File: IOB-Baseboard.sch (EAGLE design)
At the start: 72 parts, among them J1 I2C, J2 I2C, Q0 P-FET, Q1 P-FET, Q10 P-FET, Q11 P-FET, Q12 P-FET, Q13 P-FET, Q14 P-FET, Q15 P-FET, Q2 P-FET, Q3 P-FET, Q4 P-FET, Q5 P-FET, Q6 P-FET, Q7 P-FET, Q8 P-FET, Q9 P-FET

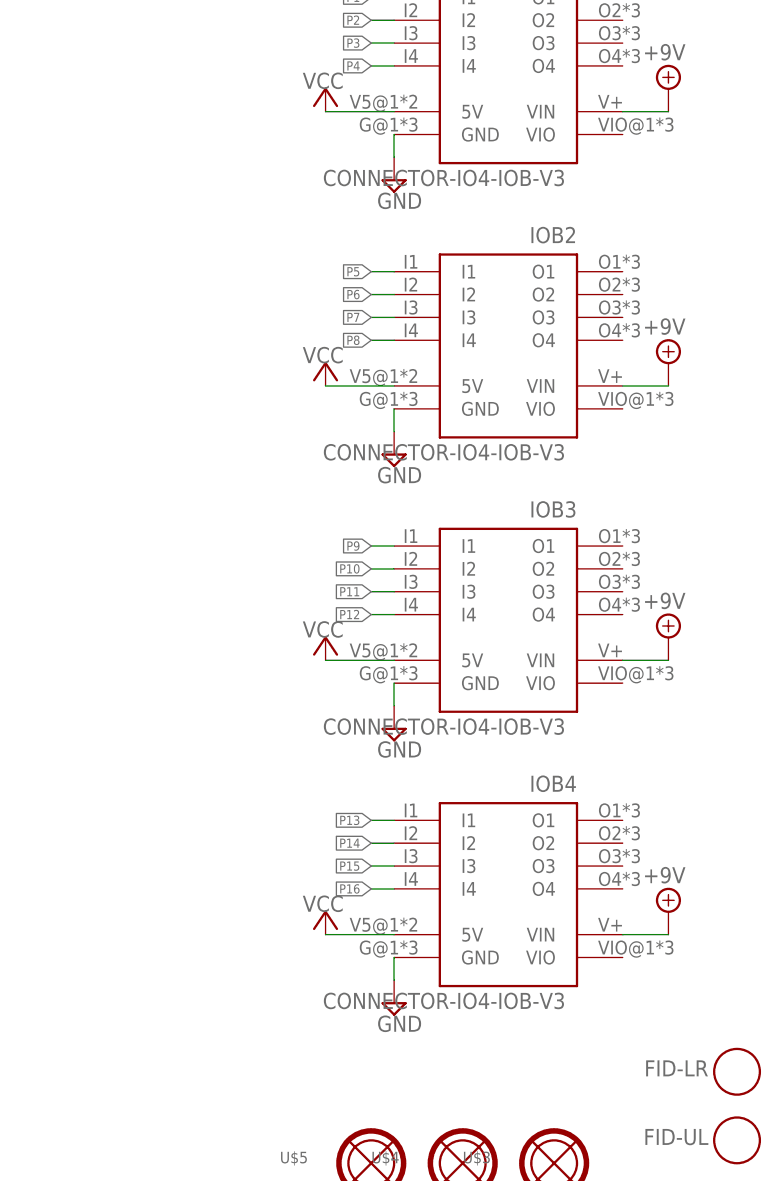
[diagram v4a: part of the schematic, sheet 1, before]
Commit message: normalized values
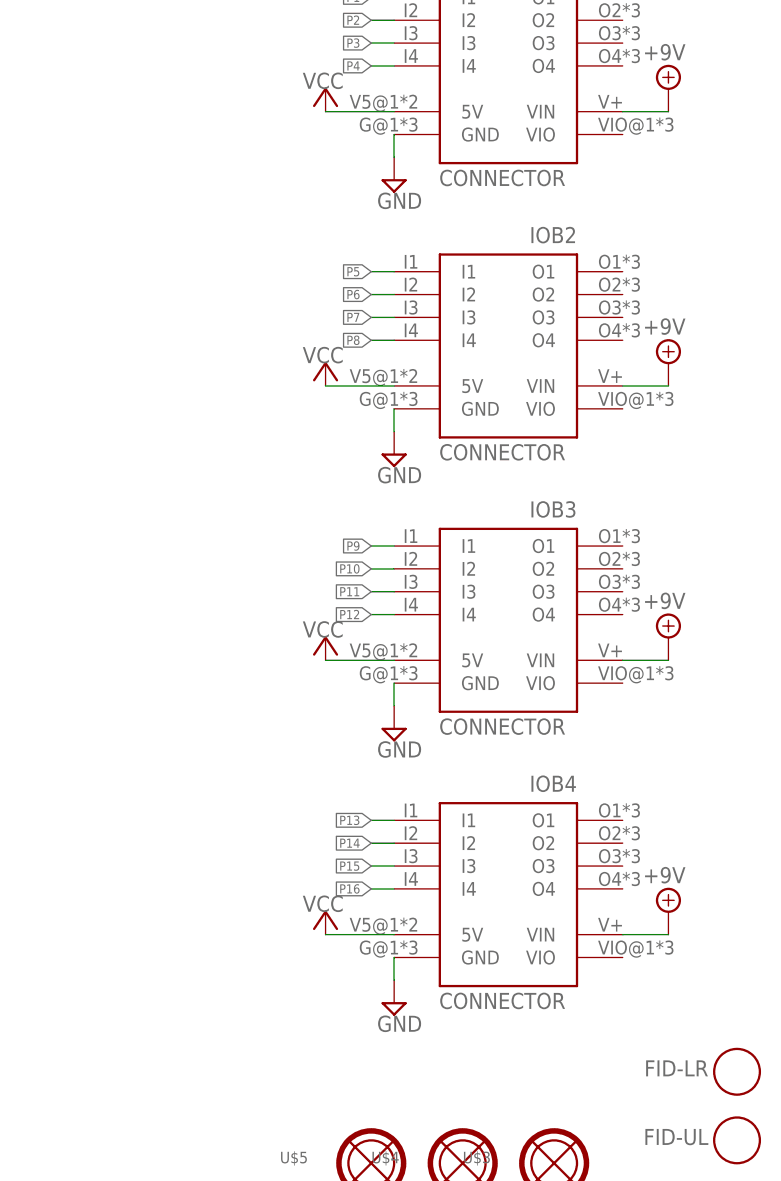
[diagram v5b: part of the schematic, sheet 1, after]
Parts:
- BOARD1: value BOARD80X100-IOB -> BOARD
- C1, C2: device SPCoast:CAP0805 -> SPCoast:CAP0603
- IOB1, IOB2, IOB3, IOB4: value CONNECTOR-IO4-IOB-V3 -> CONNECTOR
- R10, R11, R12, R13, R14, R15, R16, R18, R2, R21, R22, R4, R5, R6, R7, R8, R9: device SPCoast:R0805-RES -> SPCoast:R0603-RES
- U$1: value OSHW-LOGOL -> OSHW
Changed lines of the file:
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@@
 <parts>
 <part name="FRAME1" library="MCP" deviceset="FRAME-LETTER" device=""/>
-<part name="C1" library="SPCoast" deviceset="CAP*" device="0805" value="0.1uF"/>
-<part name="C2" library="SPCoast" deviceset="CAP*" device="0805" value="10uF"/>
+<part name="C1" library="SPCoast" deviceset="CAP*" device="0603" value="0.1uF"/>
+<part name="C2" library="SPCoast" deviceset="CAP*" device="0603" value="10uF"/>
 <part name="P+2" library="supply1" deviceset="VCC" device=""/>
-<part name="U$1" library="SparkFun" deviceset="OSHW-LOGO" device="L" value="OSHW-LOGOL"/>
+<part name="U$1" library="SparkFun" deviceset="OSHW-LOGO" device="L" value="OSHW"/>
 <part name="V1" library="supply2" deviceset="GND" device=""/>
 <part name="VR1" library="SPCoast" deviceset="VREG-?-*" device="DPAK" technology="5" value="CJ7805"/>
-<part name="R18" library="SPCoast" deviceset="R*" device="0805-RES" value="2K0"/>
+<part name="R18" library="SPCoast" deviceset="R*" device="0603-RES" value="2K0"/>
 <part name="LED18" library="SPCoast" deviceset="LED*" device="0603-LED" value="G"/>
 <part name="SUPPLY2" library="supply2" deviceset="+9V" device=""/>
@@
 <part name="J2" library="SPCoast" deviceset="CONNECTOR-I2C" device="LEFT" value="I2C"/>
 <part name="V12" library="supply2" deviceset="GND" device=""/>
-<part name="BOARD1" library="SPCoast" deviceset="BOARD" device="80X100-IOB" value="BOARD80X100-IOB"/>
+<part name="BOARD1" library="SPCoast" deviceset="BOARD" device="80X100-IOB" value="BOARD"/>
 <part name="P+3" library="supply1" deviceset="VCC" device=""/>
 <part name="V9" library="supply2" deviceset="GND" device=""/>
@@
 <part name="VIN1" library="SPCoast" deviceset="CONNECTOR-POWER" device="-L"/>
 <part name="VIN2" library="SPCoast" deviceset="CONNECTOR-POWER" device="-L" value="CONNECTOR-POWER-L"/>
-<part name="IOB1" library="SPCoast" deviceset="CONNECTOR-IO4-IOB-V3" device=""/>
+<part name="IOB1" library="SPCoast" deviceset="CONNECTOR-IO4-IOB-V3" device="" value="CONNECTOR"/>
 <part name="P+4" library="supply1" deviceset="VCC" device=""/>
 <part name="V2" library="supply2" deviceset="GND" device=""/>
 <part name="SUPPLY1" library="supply2" deviceset="+9V" device=""/>
-<part name="IOB2" library="SPCoast" deviceset="CONNECTOR-IO4-IOB-V3" device=""/>
+<part name="IOB2" library="SPCoast" deviceset="CONNECTOR-IO4-IOB-V3" device="" value="CONNECTOR"/>
 <part name="P+5" library="supply1" deviceset="VCC" device=""/>
 <part name="V3" library="supply2" deviceset="GND" device=""/>
 <part name="SUPPLY4" library="supply2" deviceset="+9V" device=""/>
-<part name="IOB3" library="SPCoast" deviceset="CONNECTOR-IO4-IOB-V3" device=""/>
+<part name="IOB3" library="SPCoast" deviceset="CONNECTOR-IO4-IOB-V3" device="" value="CONNECTOR"/>
 <part name="P+7" library="supply1" deviceset="VCC" device=""/>
 <part name="V4" library="supply2" deviceset="GND" device=""/>
 <part name="SUPPLY5" library="supply2" deviceset="+9V" device=""/>
-<part name="IOB4" library="SPCoast" deviceset="CONNECTOR-IO4-IOB-V3" device=""/>
+<part name="IOB4" library="SPCoast" deviceset="CONNECTOR-IO4-IOB-V3" device="" value="CONNECTOR"/>
 <part name="U$2" library="SPCoast" deviceset="CONNECTOR-I2C-EXPANDER" device=""/>
 <part name="V6" library="supply2" deviceset="GND" device=""/>
@@
 <part name="FRAME3" library="SPCoast" deviceset="DOC-FRAME-LETTER" device=""/>
 <part name="LED2" library="SPCoast" deviceset="LED*" device="0603-LED" value="Y"/>
-<part name="R4" library="SPCoast" deviceset="R*" device="0805-RES" value="2K0"/>
+<part name="R4" library="SPCoast" deviceset="R*" device="0603-RES" value="2K0"/>
 <part name="LED3" library="SPCoast" deviceset="LED*" device="0603-LED" value="Y"/>
-<part name="R5" library="SPCoast" deviceset="R*" device="0805-RES" value="2K0"/>
+<part name="R5" library="SPCoast" deviceset="R*" device="0603-RES" value="2K0"/>
 <part name="LED4" library="SPCoast" deviceset="LED*" device="0603-LED" value="Y"/>
-<part name="R6" library="SPCoast" deviceset="R*" device="0805-RES" value="2K0"/>
+<part name="R6" library="SPCoast" deviceset="R*" device="0603-RES" value="2K0"/>
 <part name="LED5" library="SPCoast" deviceset="LED*" device="0603-LED" value="Y"/>
-<part name="R7" library="SPCoast" deviceset="R*" device="0805-RES" value="2K0"/>
+<part name="R7" library="SPCoast" deviceset="R*" device="0603-RES" value="2K0"/>
 <part name="Q0" library="SPCoast" deviceset="MOSFET-P" device="-044021001" value="P-FET"/>
 <part name="Q1" library="SPCoast" deviceset="MOSFET-P" device="-044021001" value="P-FET"/>
@@
 <part name="P+21" library="supply1" deviceset="VCC" device=""/>
 <part name="LED6" library="SPCoast" deviceset="LED*" device="0603-LED" value="Y"/>
-<part name="R8" library="SPCoast" deviceset="R*" device="0805-RES" value="2K0"/>
+<part name="R8" library="SPCoast" deviceset="R*" device="0603-RES" value="2K0"/>
 <part name="LED7" library="SPCoast" deviceset="LED*" device="0603-LED" value="Y"/>
-<part name="R9" library="SPCoast" deviceset="R*" device="0805-RES" value="2K0"/>
+<part name="R9" library="SPCoast" deviceset="R*" device="0603-RES" value="2K0"/>
 <part name="LED8" library="SPCoast" deviceset="LED*" device="0603-LED" value="Y"/>
-<part name="R10" library="SPCoast" deviceset="R*" device="0805-RES" value="2K0"/>
+<part name="R10" library="SPCoast" deviceset="R*" device="0603-RES" value="2K0"/>
 <part name="LED9" library="SPCoast" deviceset="LED*" device="0603-LED" value="Y"/>
-<part name="R11" library="SPCoast" deviceset="R*" device="0805-RES" value="2K0"/>
+<part name="R11" library="SPCoast" deviceset="R*" device="0603-RES" value="2K0"/>
 <part name="Q4" library="SPCoast" deviceset="MOSFET-P" device="-044021001" value="P-FET"/>
 <part name="Q5" library="SPCoast" deviceset="MOSFET-P" device="-044021001" value="P-FET"/>
@@
 <part name="P+25" library="supply1" deviceset="VCC" device=""/>
 <part name="LED10" library="SPCoast" deviceset="LED*" device="0603-LED" value="Y"/>
-<part name="R12" library="SPCoast" deviceset="R*" device="0805-RES" value="2K0"/>
+<part name="R12" library="SPCoast" deviceset="R*" device="0603-RES" value="2K0"/>
 <part name="LED11" library="SPCoast" deviceset="LED*" device="0603-LED" value="Y"/>
-<part name="R13" library="SPCoast" deviceset="R*" device="0805-RES" value="2K0"/>
+<part name="R13" library="SPCoast" deviceset="R*" device="0603-RES" value="2K0"/>
 <part name="LED12" library="SPCoast" deviceset="LED*" device="0603-LED" value="Y"/>
-<part name="R14" library="SPCoast" deviceset="R*" device="0805-RES" value="2K0"/>
+<part name="R14" library="SPCoast" deviceset="R*" device="0603-RES" value="2K0"/>
 <part name="LED13" library="SPCoast" deviceset="LED*" device="0603-LED" value="Y"/>
-<part name="R15" library="SPCoast" deviceset="R*" device="0805-RES" value="2K0"/>
+<part name="R15" library="SPCoast" deviceset="R*" device="0603-RES" value="2K0"/>
 <part name="Q8" library="SPCoast" deviceset="MOSFET-P" device="-044021001" value="P-FET"/>
 <part name="Q9" library="SPCoast" deviceset="MOSFET-P" device="-044021001" value="P-FET"/>
@@
 <part name="P+29" library="supply1" deviceset="VCC" device=""/>
 <part name="LED14" library="SPCoast" deviceset="LED*" device="0603-LED" value="Y"/>
-<part name="R16" library="SPCoast" deviceset="R*" device="0805-RES" value="2K0"/>
+<part name="R16" library="SPCoast" deviceset="R*" device="0603-RES" value="2K0"/>
 <part name="LED15" library="SPCoast" deviceset="LED*" device="0603-LED" value="Y"/>
-<part name="R2" library="SPCoast" deviceset="R*" device="0805-RES" value="2K0"/>
+<part name="R2" library="SPCoast" deviceset="R*" device="0603-RES" value="2K0"/>
 <part name="LED17" library="SPCoast" deviceset="LED*" device="0603-LED" value="Y"/>
-<part name="R21" library="SPCoast" deviceset="R*" device="0805-RES" value="2K0"/>
+<part name="R21" library="SPCoast" deviceset="R*" device="0603-RES" value="2K0"/>
 <part name="LED19" library="SPCoast" deviceset="LED*" device="0603-LED" value="Y"/>
-<part name="R22" library="SPCoast" deviceset="R*" device="0805-RES" value="2K0"/>
+<part name="R22" library="SPCoast" deviceset="R*" device="0603-RES" value="2K0"/>
 <part name="Q12" library="SPCoast" deviceset="MOSFET-P" device="-044021001" value="P-FET"/>
 <part name="Q13" library="SPCoast" deviceset="MOSFET-P" device="-044021001" value="P-FET"/>
